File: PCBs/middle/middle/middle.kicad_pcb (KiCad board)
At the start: 2 copper layers, 11 parts, among them J1 Conn_01x04_Socket, J2 Conn_01x04_Socket, J3 Conn_01x04_Socket, J4 Conn_01x04_Socket, J5 Conn_01x04_Socket, J6 Conn_01x04_Socket, J7 Conn_01x02_Socket, U1 DEV-16771, U2 4754

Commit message: middle v2
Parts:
- removed F2: Fuse, Fuse:Fuseholder_Clip-5x20mm_Schurter_OG_Lateral_P15.00x5.00mm_D1.3mm_Horizontal
- added R1: 4.7k, Resistor_THT:R_Axial_DIN0207_L6.3mm_D2.5mm_P10.16mm_Horizontal, F.Cu at (129.7, 123.3)
- added R2: 1k, Resistor_THT:R_Axial_DIN0207_L6.3mm_D2.5mm_P10.16mm_Horizontal, F.Cu at (139.9, 127.0)
- moved F1 64.7 mm to (132.0, 65.0)
- moved J3 24.4 mm to (117.4, 82.8), turned to 90 degrees
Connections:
- F1 pad 2: Net-(F1-Pad2) -> Net-(J5-Pin_2)
- J5 pad 2: +5V -> Net-(J5-Pin_2)
- U1 pad 14: unconnected-(U1-A0-Pad14) -> /Vbat
- U1 pad 3.3V_1: 3.3V -> +3.3V
- U1 pad 3.3V_2: 3.3V -> +3.3V
- U1 pad 3.3V_3: 3.3V -> +3.3V
- U1 pad VIN: Net-(F1-Pad2) -> +5V

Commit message: middle revision
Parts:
- added R4: 10k, Resistor_THT:R_Axial_DIN0204_L3.6mm_D1.6mm_P5.08mm_Horizontal, F.Cu at (142.0, 132.2)
- added R5: 10k, Resistor_THT:R_Axial_DIN0204_L3.6mm_D1.6mm_P5.08mm_Horizontal, F.Cu at (131.5, 132.5)
- added R6: 10k, Resistor_THT:R_Axial_DIN0204_L3.6mm_D1.6mm_P5.08mm_Horizontal, F.Cu at (127.0, 124.1)
- added SW1: SW_Push, Button_Switch_THT:SW_PUSH_6mm_H5mm, F.Cu at (141.2, 124.7)
- added SW2: SW_Push, Button_Switch_THT:SW_PUSH_6mm_H5mm, F.Cu at (130.7, 124.8)
- added SW3: SW_Push, Button_Switch_THT:SW_PUSH_6mm_H5mm, F.Cu at (130.9, 114.5)
- added U3: RFM69HCW, RF_Module:HOPERF_RFM9XW_THT, F.Cu at (134.2, 106.6)
- R1, R2: footprint Resistor_THT:R_Axial_DIN0207_L6.3mm_D2.5mm_P10.16mm_Horizontal -> Resistor_THT:R_Axial_DIN0204_L3.6mm_D1.6mm_P5.08mm_Horizontal
- moved J6 58.3 mm to (155.7, 54.8), turned to 0 degrees
- moved R2 50.7 mm to (133.8, 76.7), turned to 0 degrees
- moved R1 46.7 mm to (126.2, 76.7)
- moved J3 39.7 mm to (154.8, 69.4)
- moved J4 38.9 mm to (162.8, 69.5)
- moved J5 27.0 mm to (130.1, 55.6)
- moved J2 15.2 mm to (130.1, 71.6)
- moved J1 14.9 mm to (130.1, 63.3)
- moved U2 14.0 mm to (137.6, 91.0), turned to 90 degrees
- moved F1 12.9 mm to (143.3, 71.2), turned to 90 degrees
- moved J7 10.5 mm to (128.1, 109.7)
- moved U1 0.20 mm to (159.0, 103.3)
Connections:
- U1 pad 20: unconnected-(U1-A6-Pad20) -> Net-(U1-A6)
- U1 pad 21: unconnected-(U1-A7-Pad21) -> Net-(U1-A7)
- U1 pad 22: unconnected-(U1-A8-Pad22) -> Net-(U1-A8)
- U1 pad 28: unconnected-(U1-RX7-Pad28) -> /CHARGE
- U1 pad 29: unconnected-(U1-TX7-Pad29) -> /KICK
- U1 pad 34: unconnected-(U1-RX8-Pad34) -> /RFMreset
- U1 pad 35: unconnected-(U1-TX8-Pad35) -> /RFM0
- U1 pad 36: /KICK -> /NSS
- U1 pad 37: /CHARGE -> unconnected-(U1-CS3-Pad37)

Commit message: mainboard layout
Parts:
- removed J1, J6: Conn_01x04_Socket, Connector_JST:JST_XH_B4B-XH-A_1x04_P2.50mm_Vertical
- removed J7: Conn_01x02_Socket, Connector_JST:JST_XH_B2B-XH-A_1x02_P2.50mm_Vertical
- added C1: 220u, Capacitor_THT:CP_Radial_D10.0mm_P3.80mm, F.Cu at (3.64, 5.28)
- added H2: MountingHole_Pad, MountingHole:MountingHole_3.2mm_M3_DIN965_Pad, F.Cu at (193.8, 45.8)
- added H3: MountingHole_Pad, MountingHole:MountingHole_3.2mm_M3_DIN965_Pad, F.Cu at (106.7, 113.9)
- added H4: MountingHole_Pad, MountingHole:MountingHole_3.2mm_M3_DIN965_Pad, F.Cu at (174.8, 45.8)
- added H5: MountingHole_Pad, MountingHole:MountingHole_3.2mm_M3_DIN965_Pad, F.Cu at (106.7, 132.9)
- added H6: MountingHole_Pad, MountingHole:MountingHole_3.2mm_M3_DIN965_Pad, F.Cu at (176.6, 115.7)
- added H7: MountingHole_Pad, MountingHole:MountingHole_3.2mm_M3_DIN965_Pad, F.Cu at (3.08, 14.6)
- added J15: Screw_Terminal_01x02, TerminalBlock_Phoenix:TerminalBlock_Phoenix_MKDS-1,5-2_1x02_P5.00mm_Horizontal, F.Cu at (150.8, 97.5)
- added J16: Screw_Terminal_01x02, TerminalBlock_Phoenix:TerminalBlock_Phoenix_MKDS-1,5-2_1x02_P5.00mm_Horizontal, F.Cu at (159.6, 113.4)
- added J17: Screw_Terminal_01x02, TerminalBlock_Phoenix:TerminalBlock_Phoenix_MKDS-1,5-2_1x02_P5.00mm_Horizontal, F.Cu at (166.8, 106.2)
- added J18: Screw_Terminal_01x02, TerminalBlock_Phoenix:TerminalBlock_Phoenix_MKDS-1,5-2_1x02_P5.00mm_Horizontal, F.Cu at (141.3, 101.3)
- added J19: Screw_Terminal_01x02, TerminalBlock_Phoenix:TerminalBlock_Phoenix_MKDS-1,5-2_1x02_P5.00mm_Horizontal, F.Cu at (131.7, 105.2)
- added J20: Screw_Terminal_01x02, TerminalBlock_Phoenix:TerminalBlock_Phoenix_MKDS-1,5-2_1x02_P5.00mm_Horizontal, F.Cu at (173.8, 55.6)
- added J21: Screw_Terminal_01x02, TerminalBlock_Phoenix:TerminalBlock_Phoenix_MKDS-1,5-2_1x02_P5.00mm_Horizontal, F.Cu at (186.9, 47.1)
- J2, J3, J4, J5: value Conn_01x04_Socket -> Screw_Terminal_01x03; footprint Connector_JST:JST_XH_B4B-XH-A_1x04_P2.50mm_Vertical -> TerminalBlock_Phoenix:TerminalBlock_Phoenix_MKDS-1,5-3_1x03_P5.00mm_Horizontal
- U1, U2, U3: moved to B.Cu
- moved R5 98.9 mm to (191.4, 53.8)
- moved R4 95.4 mm to (191.4, 50.6)
- moved R6 93.0 mm to (191.4, 56.9), turned to 0 degrees
- moved SW3 78.8 mm to (182.0, 54.6), turned to 0 degrees
- moved J4 77.4 mm to (108.1, 124.3), turned to 0 degrees
- moved U3 76.0 mm to (196.1, 62.5), turned to 180 degrees
- moved J5 69.0 mm to (123.3, 124.3)
- moved SW1 62.3 mm to (178.8, 75.0), turned to -115 degrees
- moved R2 58.8 mm to (138.9, 135.3)
- moved R1 56.8 mm to (138.9, 132.1)
- moved F1 44.8 mm to (187.3, 79.7)
- moved U2 36.6 mm to (124.5, 125.2), turned to 180 degrees
- moved J2 33.5 mm to (161.9, 82.1), turned to -115 degrees
- moved SW2 19.5 mm to (145.7, 112.5), turned to -158 degrees
- moved J3 13.7 mm to (168.4, 68.3), turned to -115 degrees
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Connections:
- F1 pad 2: Net-(J5-Pin_2) -> Net-(J19-Pin_2)
- J2 pad 1: /M3A -> /M3B
- J2 pad 2: /M3B -> /M4A
- J2 pad 3: /M4A -> /M4B
- J3 pad 1: /CHARGE -> /M2A
- J3 pad 2: /KICK -> /M2B
- J3 pad 3: VCC -> /M3A
- J4 pad 1: /SCL1 -> /SS
- J4 pad 2: /SDA1 -> +5V
- J5 pad 1: VCC -> /MOSI
- J5 pad 2: Net-(J5-Pin_2) -> /MISO
- J5 pad 3: GND -> /SCLK
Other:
- board outline added: 95.1 x 95.1 mm

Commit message: e
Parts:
- removed J20: Screw_Terminal_01x02, TerminalBlock_Phoenix:TerminalBlock_Phoenix_MKDS-1,5-2_1x02_P5.00mm_Horizontal
- U3: moved to F.Cu
- moved J21 89.5 mm to (147.3, 127.4), turned to 45 degrees
- moved J19 80.6 mm to (187.2, 46.7), turned to 180 degrees
- moved J5 48.7 mm to (168.3, 105.6), turned to -135 degrees
- moved SW3 45.4 mm to (155.8, 91.7)
- moved R4 41.5 mm to (165.6, 83.1)
- moved R5 41.2 mm to (165.6, 85.8)
- moved R6 40.7 mm to (165.6, 88.4)
- moved J18 38.3 mm to (108.3, 120.9), turned to -90 degrees
- moved J17 35.0 mm to (131.8, 105.2), turned to -158 degrees
- moved J4 22.2 mm to (130.3, 124.4), turned to 180 degrees
- moved J16 21.9 mm to (141.3, 101.4), turned to -158 degrees
- moved SW1 17.2 mm to (163.0, 81.7)
- moved J3 15.9 mm to (174.5, 53.6)
- moved J2 15.9 mm to (168.0, 67.4)
- moved U3 15.9 mm to (182.6, 54.2), turned to 0 degrees
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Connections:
- F1 pad 2: Net-(J19-Pin_2) -> Net-(J18-Pin_1)
- J18 pad 1: GND -> Net-(J18-Pin_1)
- J19 pad 2: Net-(J19-Pin_2) -> GND

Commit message: e
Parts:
- removed C1: 220u, Capacitor_THT:CP_Radial_D10.0mm_P3.80mm
- removed H7: MountingHole_Pad, MountingHole:MountingHole_3.2mm_M3_DIN965_Pad

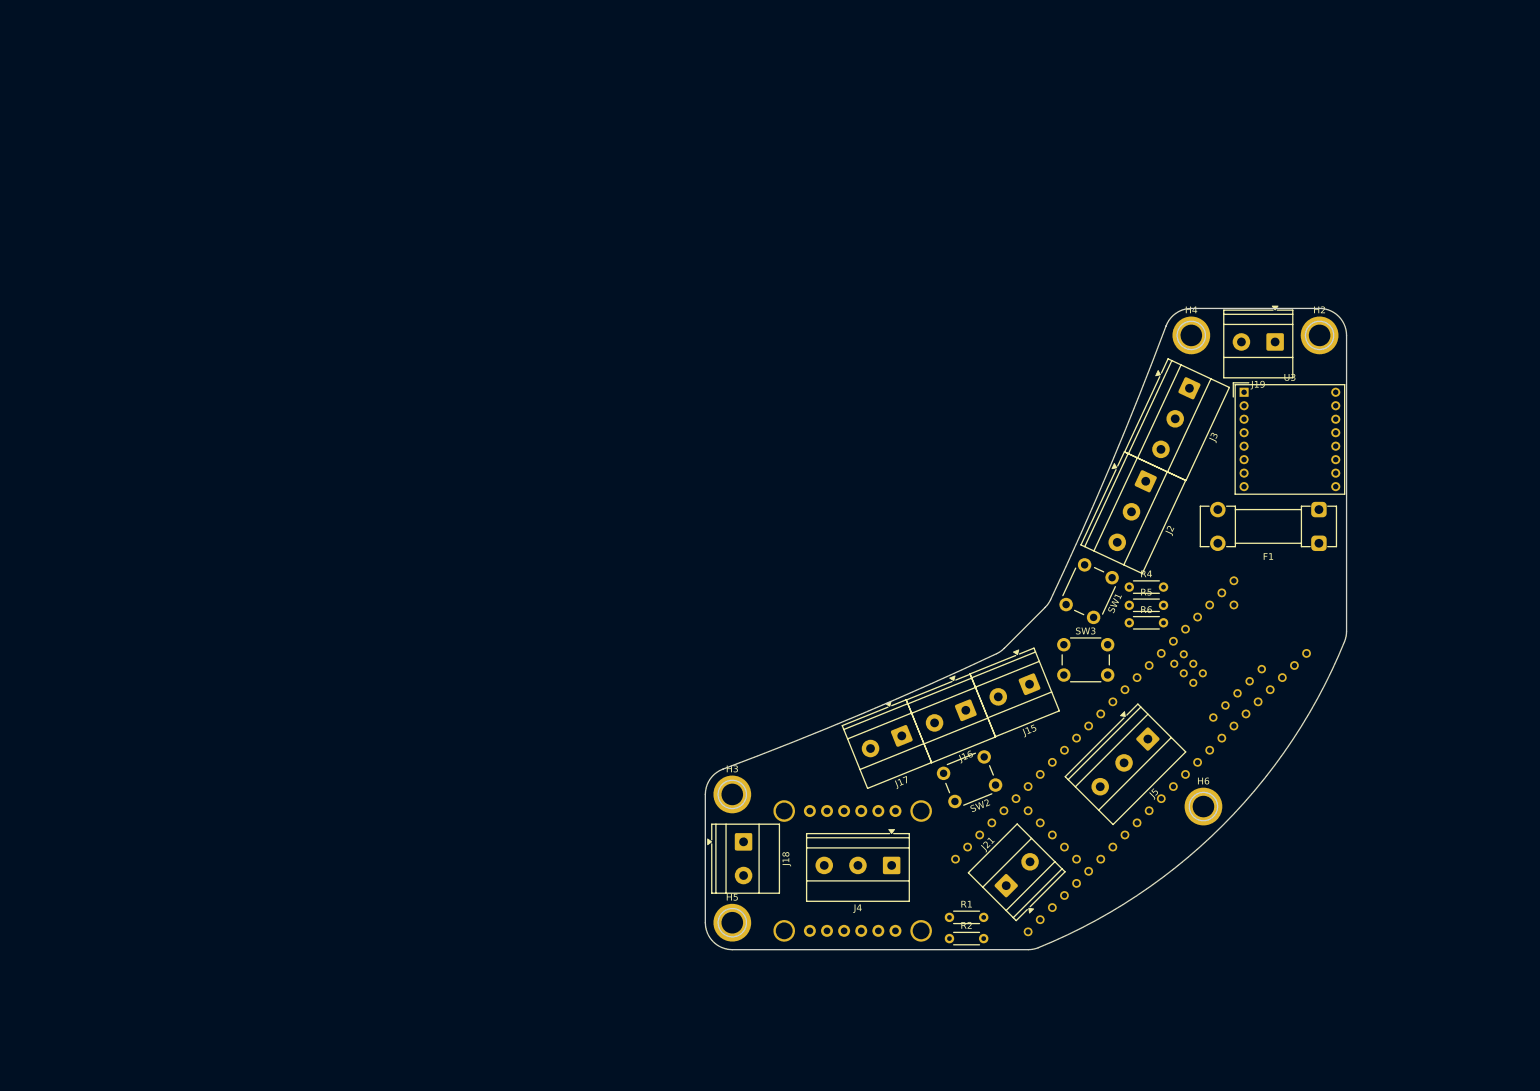
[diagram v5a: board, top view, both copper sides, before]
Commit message: middle BANANA board layout, wiring
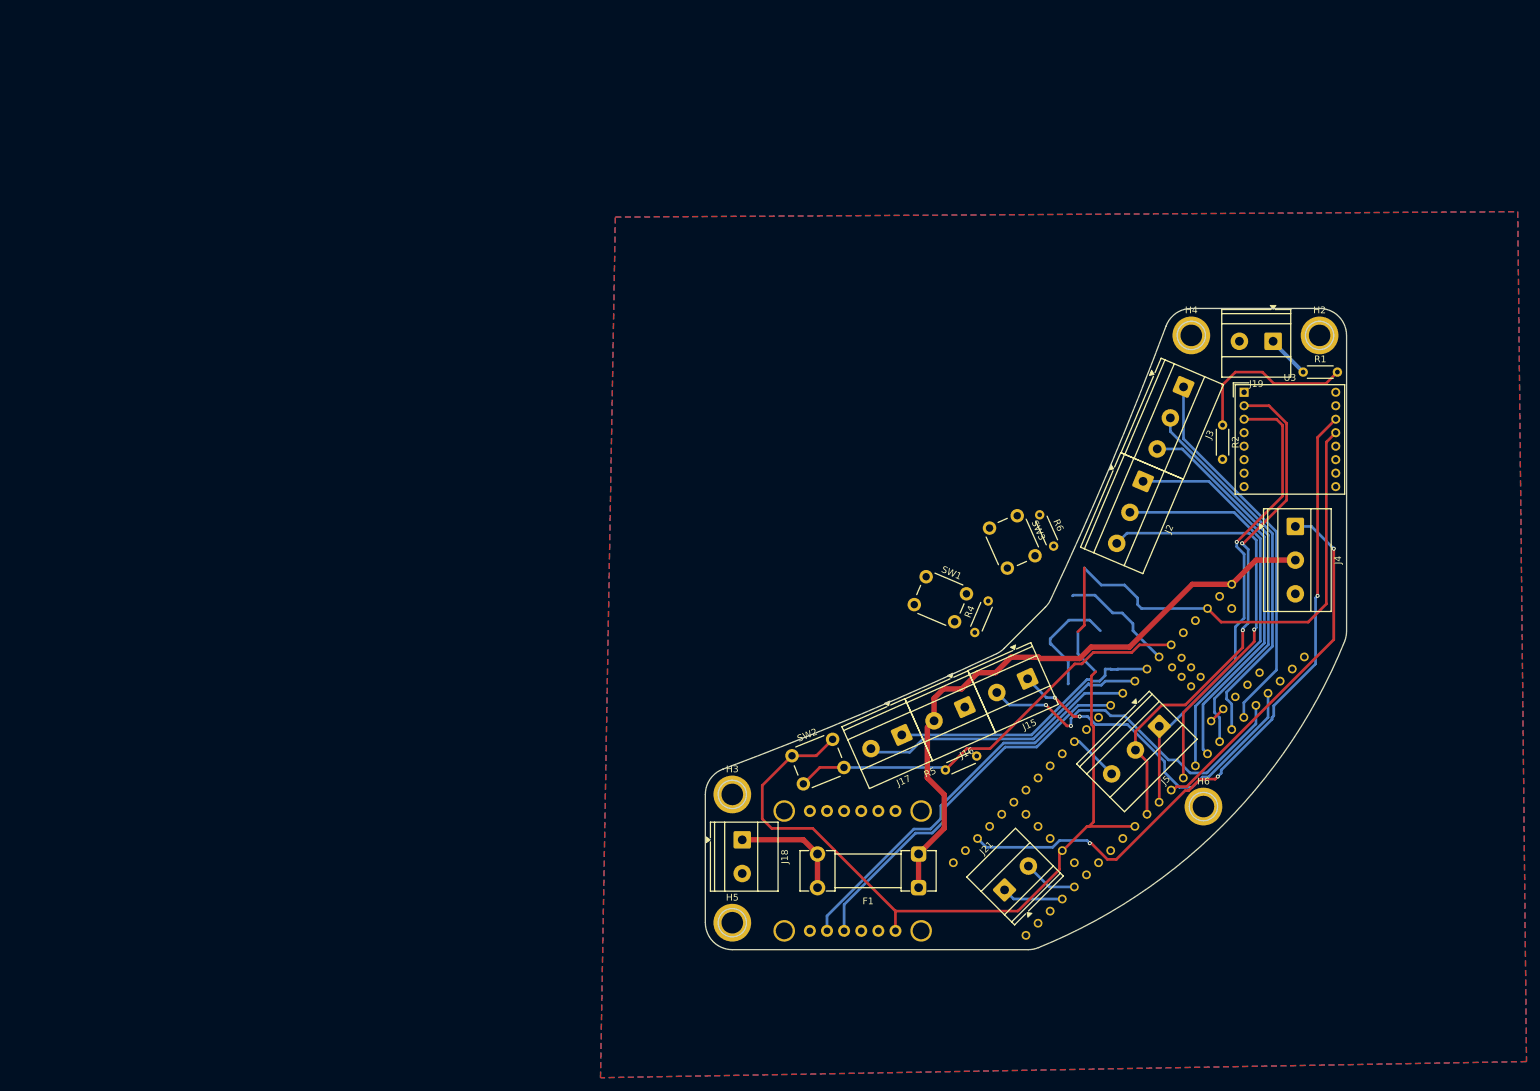
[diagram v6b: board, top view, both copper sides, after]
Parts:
- moved R1 96.4 mm to (191.4, 51.2)
- moved R2 86.3 mm to (179.4, 59.1), turned to -90 degrees
- moved F1 78.4 mm to (134.3, 127.7)
- moved J4 78.2 mm to (190.2, 74.1), turned to -90 degrees
- moved R5 36.6 mm to (138.3, 110.2), turned to 24 degrees
- moved SW2 30.5 mm to (115.5, 108.1), turned to 22 degrees
- moved SW1 27.6 mm to (135.4, 81.6), turned to -23 degrees
- moved R4 23.9 mm to (142.6, 89.8), turned to 67 degrees
- moved R6 20.8 mm to (152.3, 72.4), turned to -66 degrees
- moved SW3 20.3 mm to (148.9, 72.5), turned to -66 degrees
- moved J5 2.55 mm to (170.0, 103.7)
- moved J3 0.90 mm to (173.6, 53.4), turned to -113 degrees
- moved J15 0.85 mm to (150.5, 96.7), turned to -156 degrees
- moved J21 0.68 mm to (147.1, 128.0)
- moved U1 0.62 mm to (165.5, 108.7)
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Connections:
- J21 pad 1: /CHARGE -> /KICK
- J21 pad 2: /KICK -> /CHARGE
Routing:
- net +3.3V: track 0.00 -> 196.2 mm
- net /RFM0: track 0.00 -> 103.1 mm, vias 0 -> 3
- net +5V: track 0.00 -> 93.4 mm
- net /MISO: track 0.00 -> 78.3 mm, vias 0 -> 2
- net /MOSI: track 0.00 -> 71.5 mm, vias 0 -> 1
- net Net-(U1-A7): track 0.00 -> 63.4 mm
- net /M4B: track 0.00 -> 61.5 mm, vias 0 -> 1
- net /SDA2: track 0.00 -> 60.9 mm
- net /M4A: track 0.00 -> 58.7 mm
- net /M3B: track 0.00 -> 57.6 mm
- net /SCL2: track 0.00 -> 56.8 mm
- net /M2A: track 0.00 -> 56.8 mm
- net /M3A: track 0.00 -> 56.1 mm
- net /M2B: track 0.00 -> 55.6 mm
- net /SS: track 0.00 -> 53.9 mm, vias 0 -> 1
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- added copper zone on B.Cu, net GND
- added copper zone on F.Cu, net GND

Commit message: middle update
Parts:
- moved SW1 27.1 mm to (159.7, 93.5), turned to 157 degrees
- moved R4 21.7 mm to (164.3, 90.0), turned to -113 degrees
- moved SW3 19.6 mm to (162.7, 86.4), turned to 157 degrees
- moved R6 18.5 mm to (167.3, 83.2), turned to -113 degrees
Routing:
- net /RFMreset: track 0.00 -> 106.9 mm
- net /NSS: track 0.00 -> 83.3 mm, vias 0 -> 2
- net /Vbat: track 25.2 -> 97.3 mm, vias 0 -> 3
- net /SCLK: track 7.51 -> 67.9 mm, vias 0 -> 2
- net Net-(U1-A8): track 17.2 -> 23.5 mm, vias 0 -> 1
- net Net-(U1-A6): track 17.3 -> 23.4 mm
- net +3.3V: track 196.2 -> 197.6 mm
- net /SCL1: track 41.2 -> 40.4 mm
- net Net-(U1-A7): track 63.4 -> 63.5 mm, vias 0 -> 1
- net GND: vias 0 -> 10

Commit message: main update
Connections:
- J17 pad 1: /SCL1 -> /TX
- J17 pad 2: /SDA1 -> /RX
- U1 pad 14: /Vbat -> /RX
- U1 pad 15: unconnected-(U1-A1-Pad15) -> /TX
- U1 pad 16: /SCL2 -> /Vbat
- U1 pad 17: /SDA2 -> unconnected-(U1-A3-Pad17)
- U2 pad JP1_4: /SCL2 -> /SCL1
- U2 pad JP1_5: /SDA2 -> /SDA1
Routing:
- net +5V: track 93.6 -> 5.00 mm
- net /SDA2: track 60.9 -> 0.00 mm
- net /SCL2: track 56.8 -> 0.00 mm
- net /RX: track 0.00 -> 33.6 mm
- net /TX: track 0.00 -> 31.7 mm
- net /SCL1: track 40.4 -> 63.6 mm, vias 0 -> 1
- net /SDA1: track 43.7 -> 62.7 mm
- net /RFM0: track 103.1 -> 120.7 mm, vias 3 -> 0
- net /M1A: track 51.2 -> 37.7 mm, vias 2 -> 0
- net /M1B: track 51.7 -> 39.8 mm, vias 2 -> 0
- net /RFMreset: track 106.9 -> 95.5 mm
- net /Vbat: track 97.3 -> 86.2 mm, vias 3 -> 1
- net /SS: track 53.9 -> 46.7 mm, vias 1 -> 0
- net Net-(U1-A6): track 23.4 -> 17.2 mm
- net /M4B: track 61.3 -> 56.1 mm
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- added copper zone on In1.Cu, net +5V
- added copper zone on In2.Cu, net GND
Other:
- copper layers 2 -> 4
- board text added: "5V GND"
- board text added: "5V power fuse"
- board text added: "GND"
- board text added: "GND 5Vin"
- board text added: "KICK-> CHARGE"
- board text added: "M1"
- board text added: "M2"
- board text added: "M3"
- board text added: "M4"
- board text added: "RX TX"
- board text added: "SCLK MISO MOSI"
- board text added: "SS 5V GND"
- board text added: "Vbat"
